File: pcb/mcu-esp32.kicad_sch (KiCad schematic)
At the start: 12 parts, among them Q6 BSS138, Q9 BSS138, U10 ESP32-S3-WROOM-1-N8R8

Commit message: change some 0805s to 0603
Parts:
- renumbered C52 to C32, C30 to C33, C53 to C34, D4 to D3, Q6 to Q4, Q9 to Q5, R44 to R26, R43 to R27, R32 to R28, R33 to R29

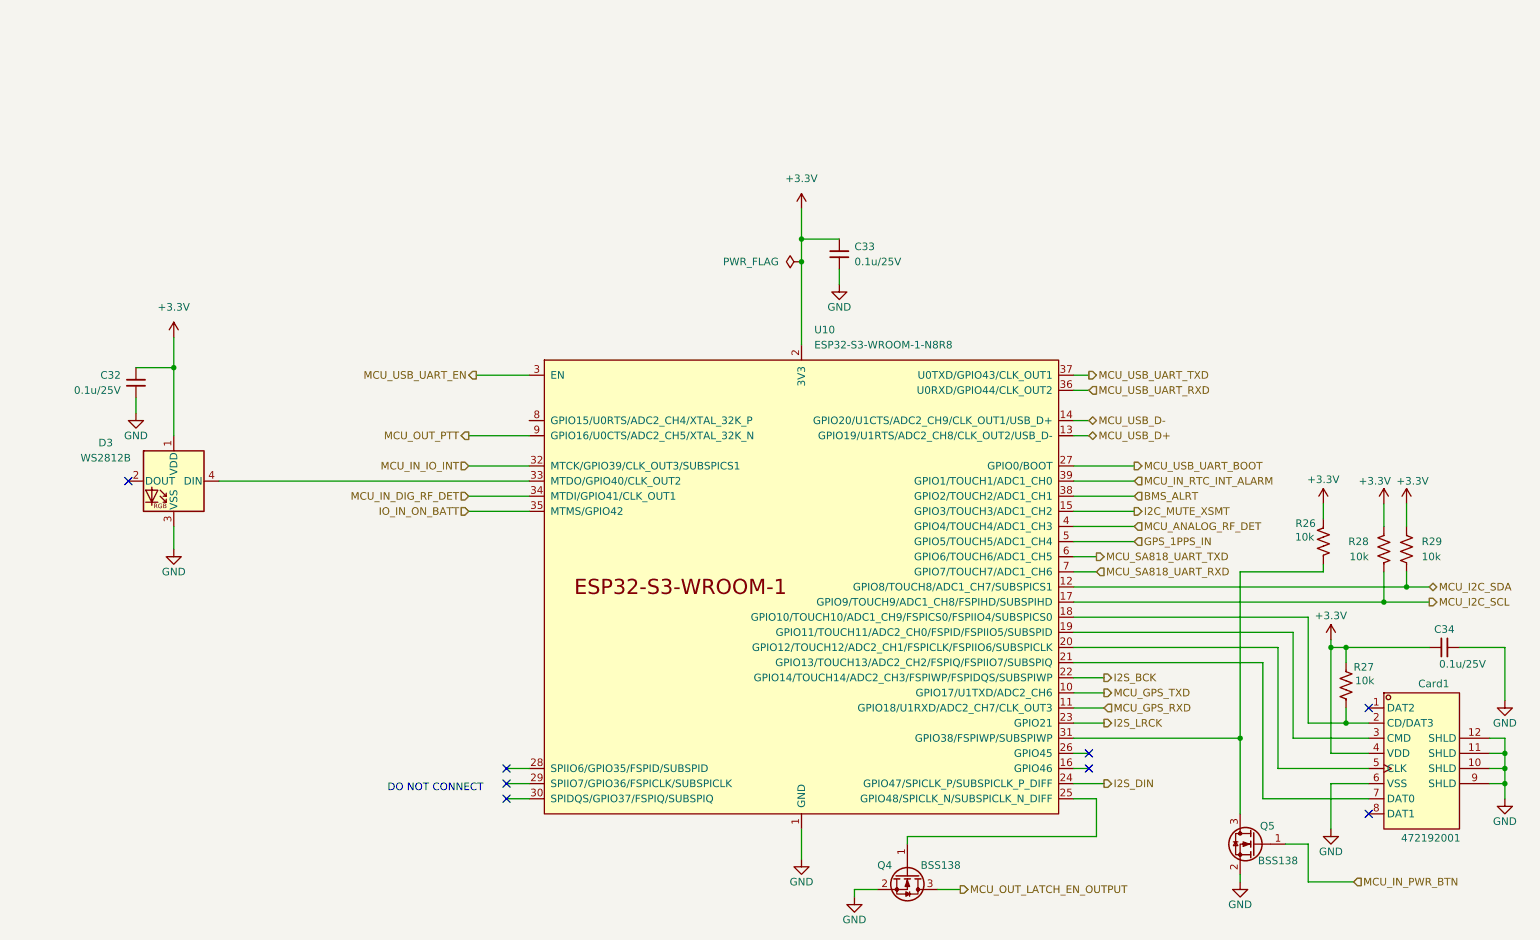
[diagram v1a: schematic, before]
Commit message: add matching network
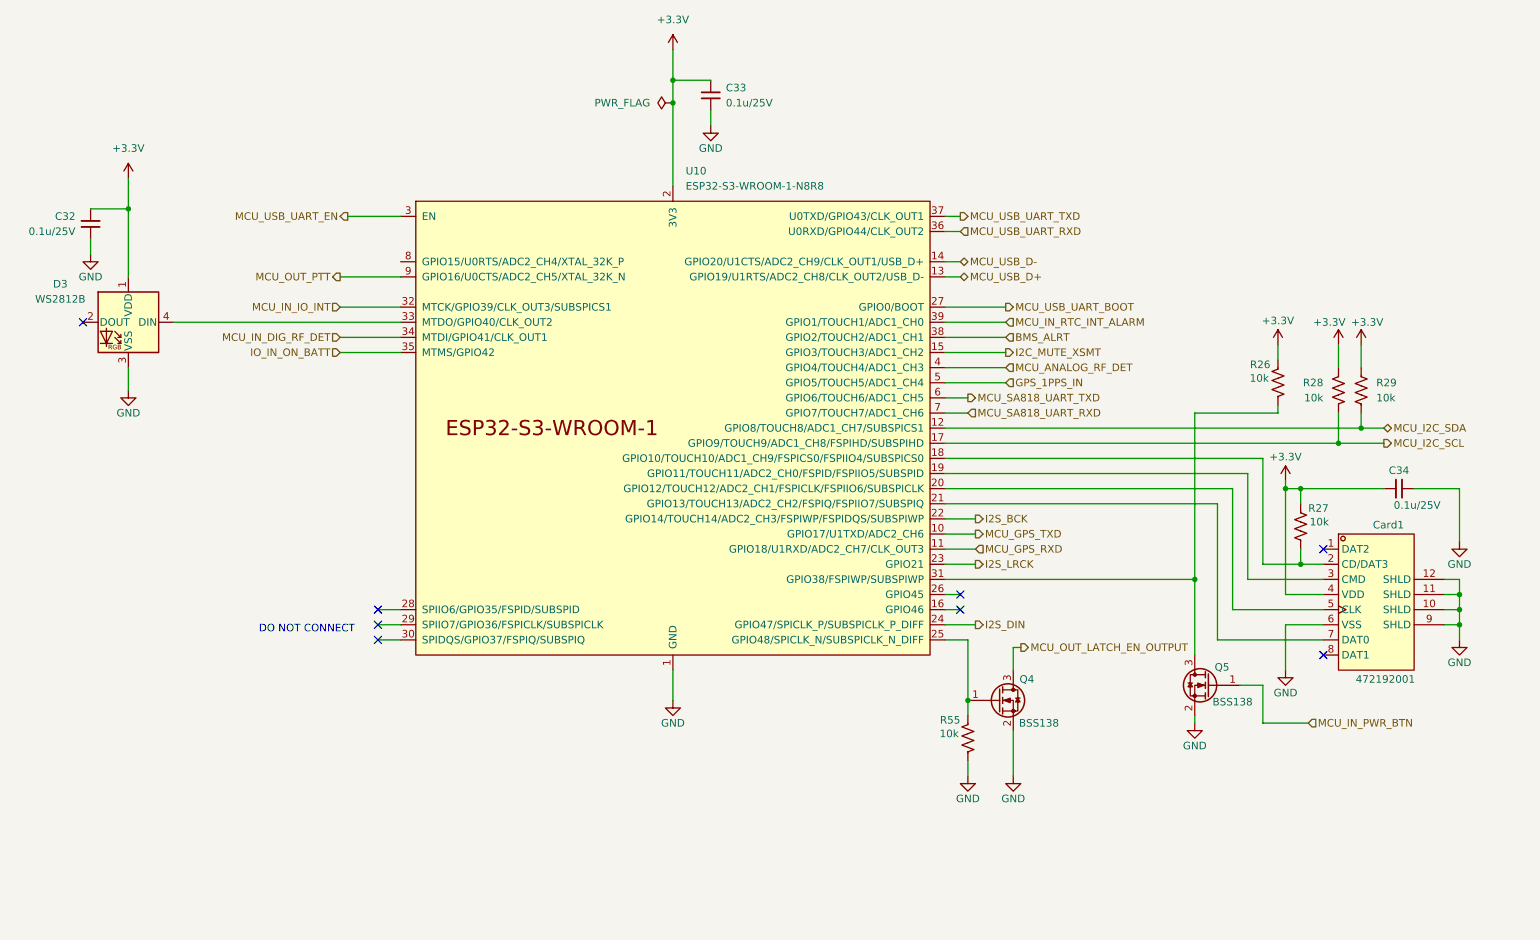
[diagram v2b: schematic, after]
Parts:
- added R55: 10k, Resistor_SMD:R_0603_1608Metric, symbol Device:R_US
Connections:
- net GND: now also R55.1
- net at Q4.1 (G), U10.25 (GPIO48/SPICLK_N/SUBSPICLK_N_DIFF): now also R55.2
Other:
- moved on the sheet: C32, C33, C34, Card1, D3, Q4, Q5, R26, R27, R28, R29, U10
